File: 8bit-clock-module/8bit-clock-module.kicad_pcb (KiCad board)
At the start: 2 copper layers, 21 parts, among them J1 Conn_01x05, SW1 SW_Push, SW2 SW_SPDT, U1 74LS08, U2 74LS04, U3 74LS32, U4 LM555, U5 LM555, U6 LM555

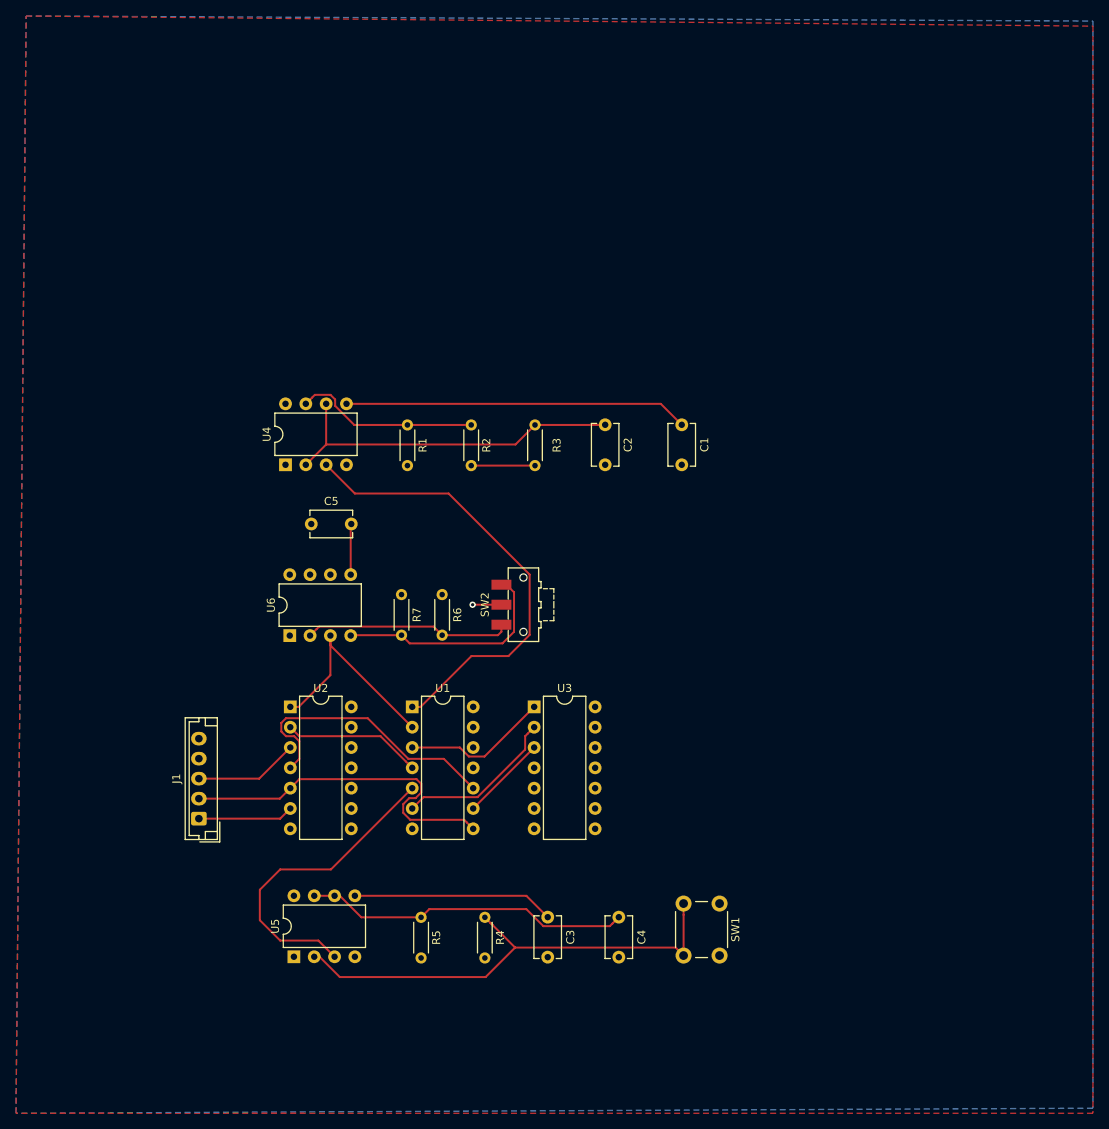
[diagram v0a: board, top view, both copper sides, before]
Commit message: Got no unconnected pins
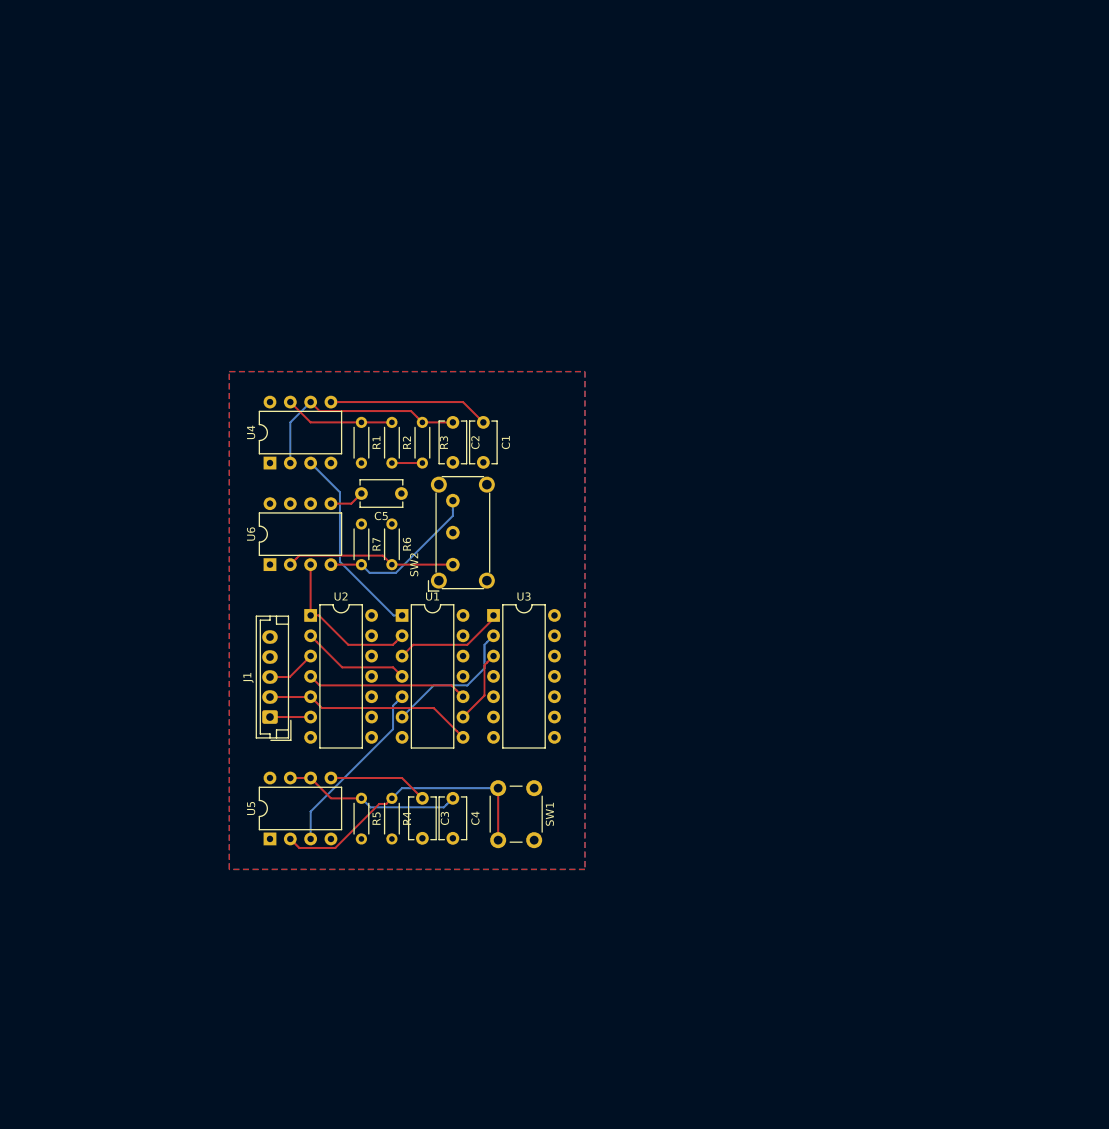
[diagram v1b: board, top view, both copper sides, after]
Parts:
- SW2: footprint Button_Switch_SMD:SW_SPDT_CK-JS102011SAQN -> Button_Switch_THT:SW_E-Switch_EG1224_SPDT_Angled
- moved SW1 27.3 mm to (104.1, 125.7)
- moved C4 25.5 mm to (94.0, 127.0)
- moved C1 24.8 mm to (97.8, 80.0)
- moved C3 21.6 mm to (90.2, 127.0)
- moved C2 19.0 mm to (94.0, 80.0)
- moved R4 18.9 mm to (86.4, 127.0)
- moved R5 16.6 mm to (82.5, 127.0)
- moved J1 15.5 mm to (71.1, 116.8)
- moved U5 15.0 mm to (71.1, 132.1)
- moved R3 14.1 mm to (90.2, 85.1)
- moved U3 12.5 mm to (99.1, 104.1)
- moved U2 11.7 mm to (76.2, 104.1)
- moved U1 11.5 mm to (87.6, 104.1)
- moved R6 10.8 mm to (86.4, 97.8)
- moved R7 10.1 mm to (82.5, 97.8)
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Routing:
- net Net-(U1-Pad1): track 57.1 -> 24.4 mm
- net Net-(R4-Pad1): track 60.8 -> 36.0 mm
- net Net-(C1-Pad1): track 43.0 -> 20.1 mm
- net Net-(C4-Pad1): track 40.3 -> 22.3 mm
- net /CLK: track 43.6 -> 26.3 mm
- net Net-(C2-Pad1): track 44.6 -> 27.5 mm
- net Net-(U1-Pad5): track 39.4 -> 22.5 mm
- net Net-(U1-Pad10): track 35.5 -> 20.1 mm
- net Net-(C3-Pad1): track 24.6 -> 12.5 mm
- net Net-(R1-Pad1): track 23.2 -> 13.8 mm
- net Net-(R7-Pad1): track 28.4 -> 20.5 mm
- net Net-(U1-Pad2): track 27.3 -> 19.8 mm
- net /HLT: track 13.0 -> 6.17 mm
- net /ICLK: track 12.0 -> 5.08 mm
- net Net-(R6-Pad1): track 25.9 -> 21.3 mm
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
